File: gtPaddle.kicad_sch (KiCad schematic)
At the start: 21 parts, among them IC1 74157N, IC2 74157N, Q9 2N3904, U1 ADC0804LCN

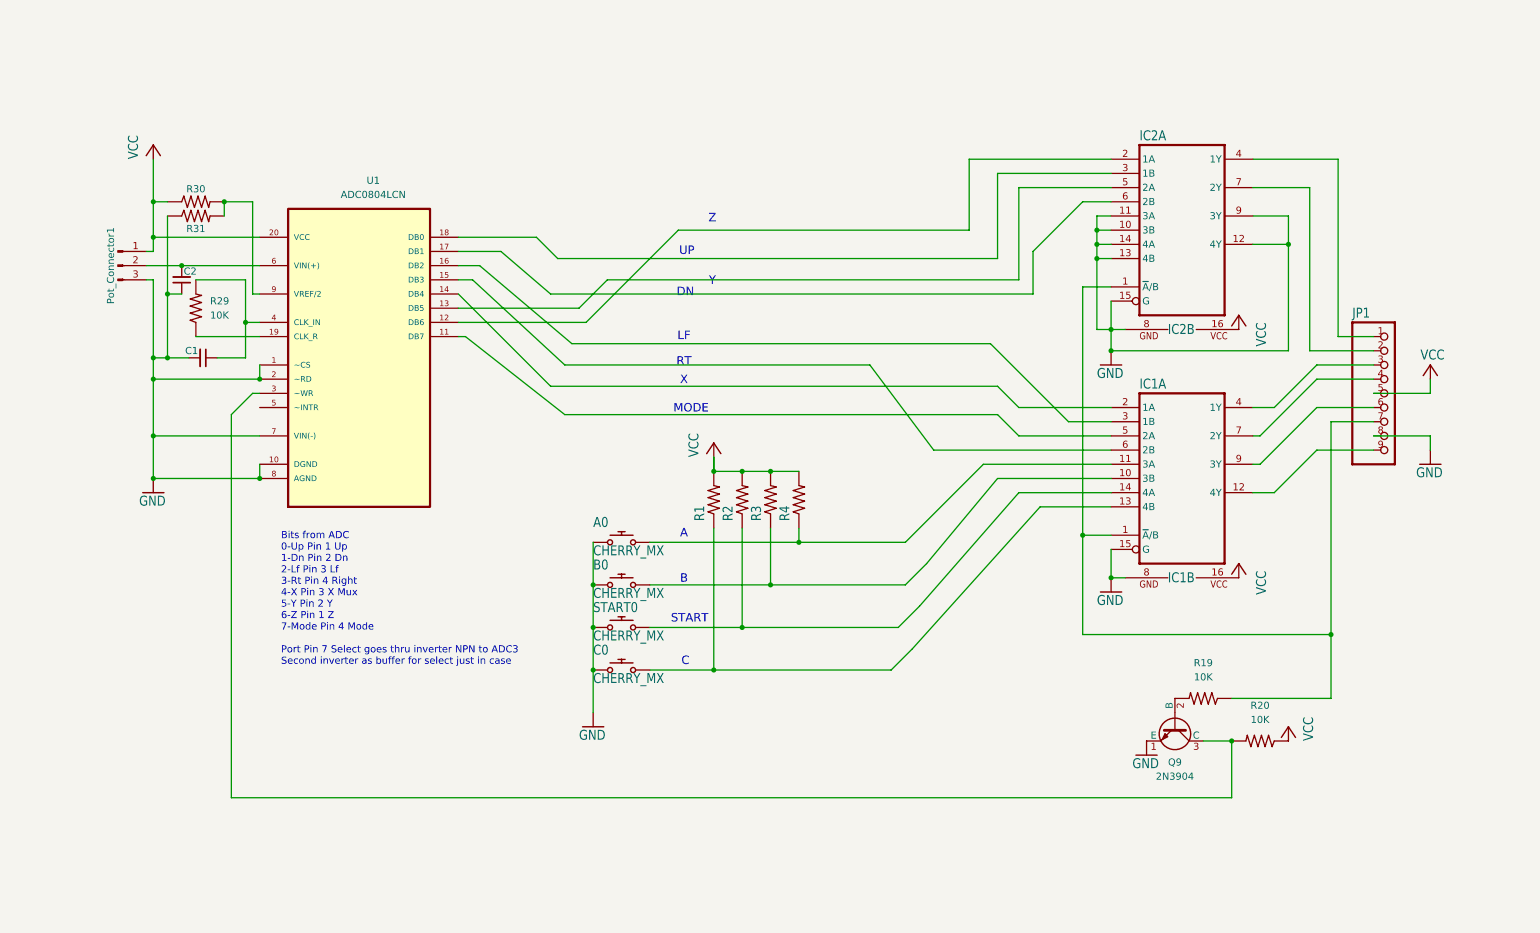
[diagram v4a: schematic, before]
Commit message: Gemini helped me update my schematic. pullups on unused mux inputs and unused outputs left floating decoupling caps on each IC. Faster switching on the inverter for earlier ADC triggering
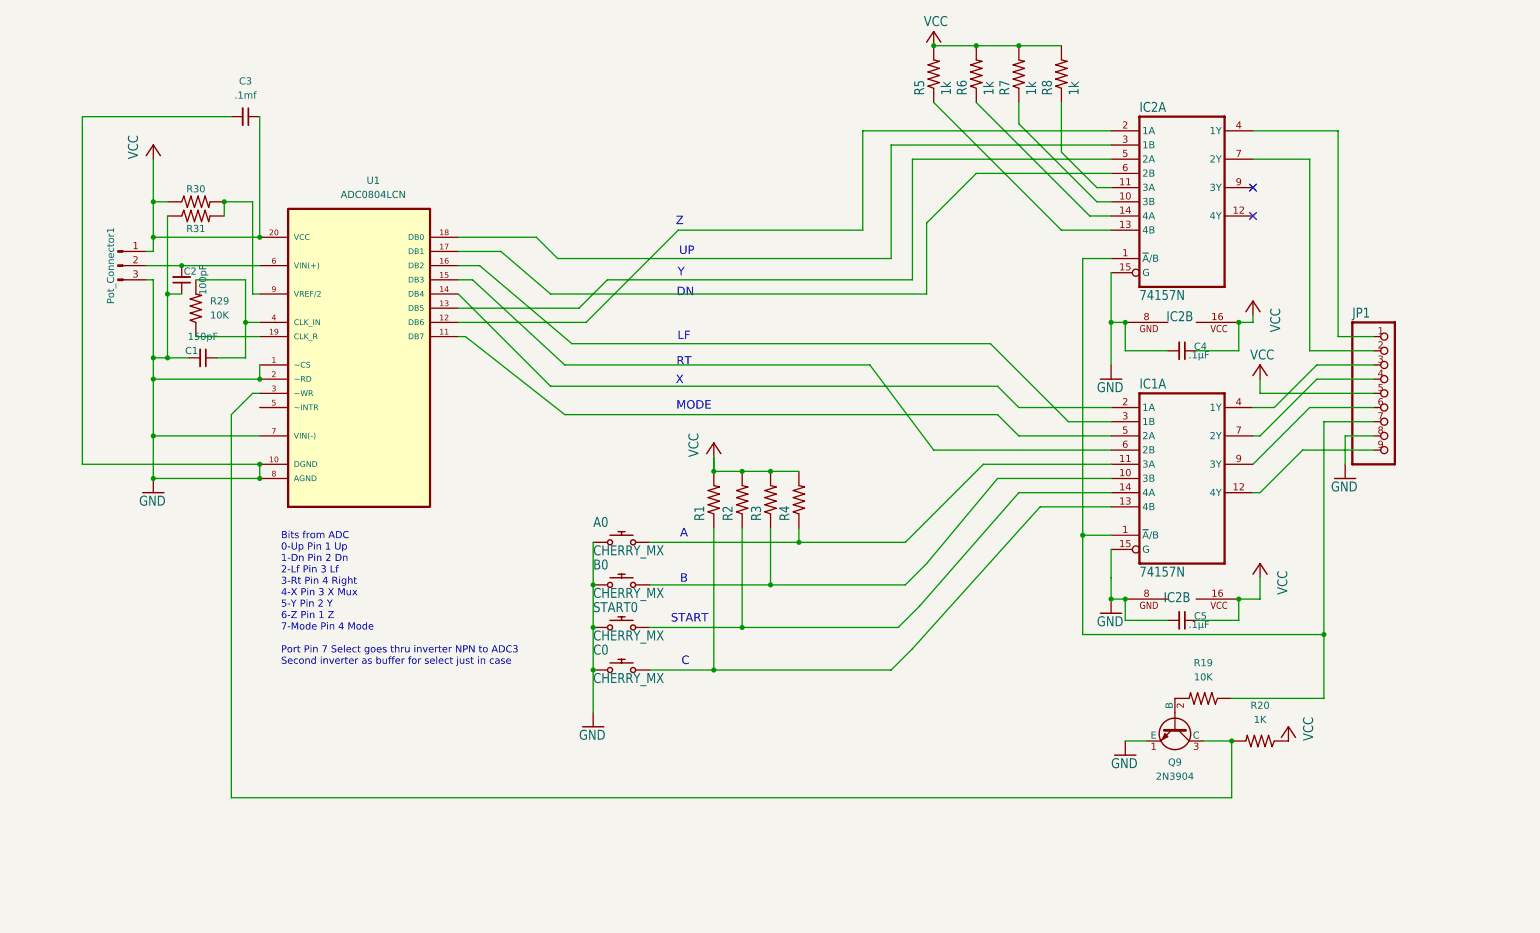
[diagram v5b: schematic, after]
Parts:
- added C3: .1mf, symbol Device:C_Small
- added C4, C5: .1µF, symbol Device:C_Small
- added R5, R6, R7, R8: 1k, gpad1:0207_10, symbol gpad1-eagle-import:R-US_0207/10
- R20: value 10K -> 1K
- renumbered IC1 to IC2
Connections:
- net GND: now also C3.2, C4.2, C5.2; no longer IC2.10 (3B), IC2.11 (3A), IC2.12 (4Y), IC2.13 (4B), IC2.14 (4A), IC2.9 (3Y)
- net VCC: now also C3.1, C4.1, C5.1, R5.2, R6.2, R7.2, R8.2
- new net: IC2.11 (3A), R8.1
- new net: IC2.14 (4A), R6.1
- new net: IC2.13 (4B), R5.1
- new net: IC2.10 (3B), R7.1
- no-connect marks 0 -> 2
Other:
- moved on the sheet: IC2A, IC2B

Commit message: capacitor notes added
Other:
- note added: "Cap values: C1 150pF code 151 - alt 220 pF - ADC clock timing 220 maybe more appropriate for 60fps C2 0.1µF code 104 - alt 100pF code 101 - Analog Signal Smoothing C3, C4, C5 - 0.1µF code 104 - Power Decoupling standard"
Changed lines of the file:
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@@
+		)
+	)
+	(text "Cap values:\nC1 150pF code 151 - alt 220 pF - ADC clock timing 220 maybe more appropriate for 60fps\nC2 0.1µF code 104 - alt 100pF code 101 - Analog Signal Smoothing\nC3, C4, C5 - 0.1µF code 104 - Power Decoupling standard"
+		(exclude_from_sim no)
+		(at 29.718 167.894 0)
+		(effects
+			(font
+				(size 1.27 1.27)
+			)
+			(justify left)
 		)
 	)

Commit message: picking cap values that are easier to stock, and use common values
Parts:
- C1: value 150pF -> 220pF
- C2: value 100pF -> .1µF
- C3: value .1mf -> .1µF; footprint (none) -> Capacitor_THT:CP_Radial_D4.0mm_P1.50mm
- C4, C5: footprint (none) -> Capacitor_THT:CP_Radial_D4.0mm_P1.50mm
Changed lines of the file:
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@@
 			)
 		)
-		(property "Footprint" ""
+		(property "Footprint" "Capacitor_THT:CP_Radial_D4.0mm_P1.50mm"
 			(at 223.52 74.93 0)
 			(effects
@@
 			)
 		)
-		(property "Value" "150pF"
+		(property "Value" "220pF"
 			(at 48.2536 72.39 90)
 			(effects
@@
 			)
 		)
-		(property "Footprint" ""
+		(property "Footprint" "Capacitor_THT:CP_Radial_D4.0mm_P1.50mm"
 			(at 223.52 123.19 0)
 			(effects
@@
 			)
 		)
-		(property "Value" "100pF"
+		(property "Value" ".1µF"
 			(at 48.26 62.2236 90)
 			(effects
@@
 			)
 		)
-		(property "Value" ".1mf"
+		(property "Value" ".1µF"
 			(at 55.8736 29.21 90)
 			(effects
@@
 			)
 		)
-		(property "Footprint" ""
+		(property "Footprint" "Capacitor_THT:CP_Radial_D4.0mm_P1.50mm"
 			(at 55.88 33.02 0)
 			(effects

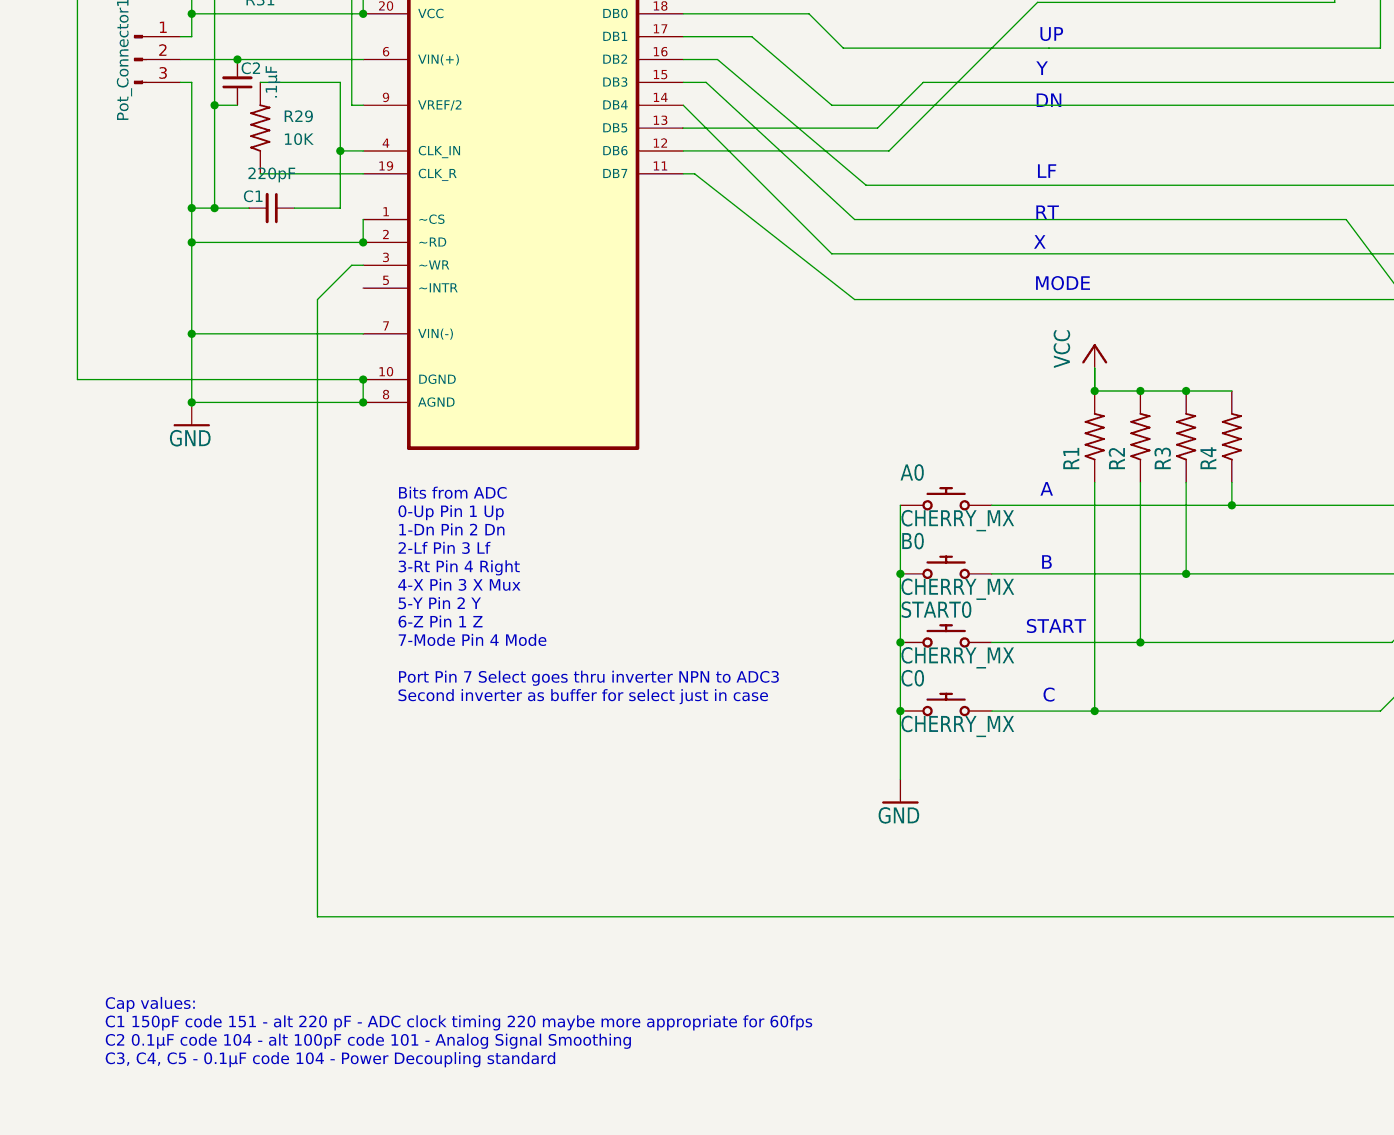
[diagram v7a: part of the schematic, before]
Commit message: swapped JST connectors for buttons
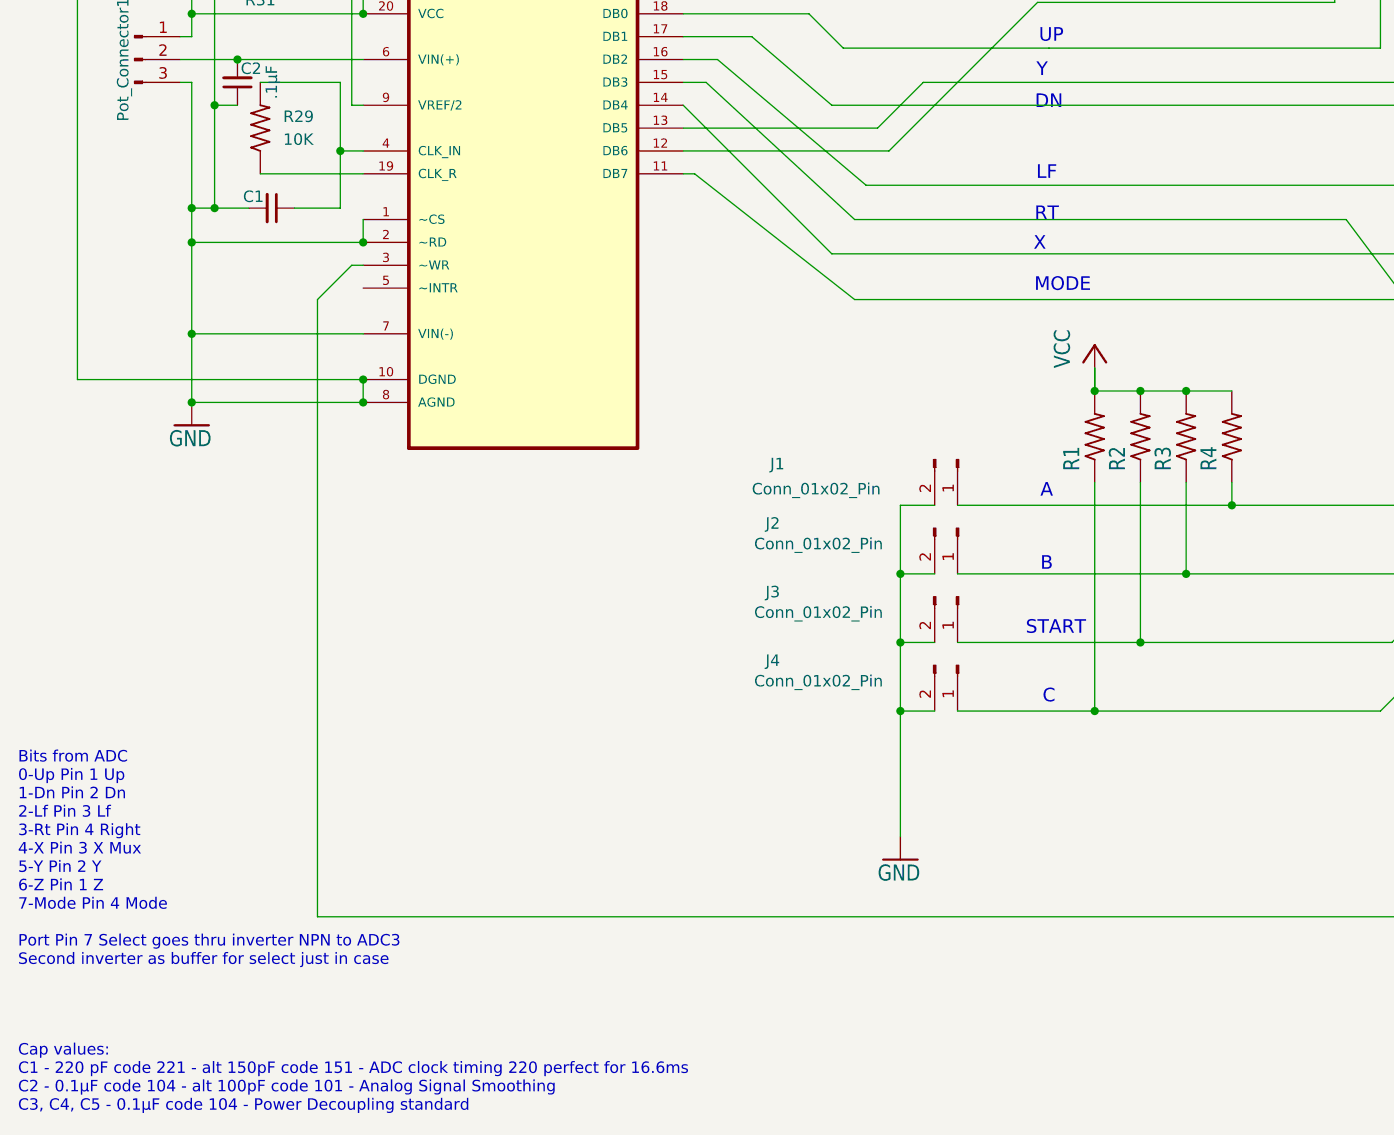
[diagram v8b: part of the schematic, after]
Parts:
- removed A0, B0, C0, START0: CHERRY_MX, gpad1:CHERRY_MX, symbol gpad1-eagle-import:CHERRY_MX
- added J1, J2, J3, J4: Conn_01x02_Pin, symbol Connector:Conn_01x02_Pin
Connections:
- net GND: now also J1.2 (Pin_2), J2.2 (Pin_2), J3.2 (Pin_2), J4.2 (Pin_2)
- net at IC1.10 (3B), R3.1: now also J2.1 (Pin_1)
- net at IC1.14 (4A), R2.1: now also J3.1 (Pin_1)
- net at IC1.13 (4B), R1.1: now also J4.1 (Pin_1)
- net at IC1.11 (3A), R4.1: now also J1.1 (Pin_1)
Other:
- note added: "Cap values: C1 - 220 pF code 221 - alt 150pF code 151 - ADC clock timing 220 perfect for 16.6ms C2 - 0.1µF code 104 - alt 100pF code 101 - Analog Signal Smoothing C3, C4, C5 - 0.1µF code 104 - Power Decoupling standard"
- note removed: "Cap values: C1 150pF code 151 - alt 220 pF - ADC clock timing 220 maybe more appropriate for 60fps C2 0.1µF code 104 - alt 100pF code 101 - Analog Signal Smoothing C3, C4, C5 - 0.1µF code 104 - Power Decoupling standard"
